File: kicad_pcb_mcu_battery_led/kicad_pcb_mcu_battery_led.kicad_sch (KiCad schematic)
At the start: 32 parts, among them J1 USB_B_Micro, J2 Test points, J3 USART, J4 ST-Link, J5 SWD, SW1 SW_Push, SW2 SW_SPDT, U1 STM32F030C6, Y1 32k, Y2 16M

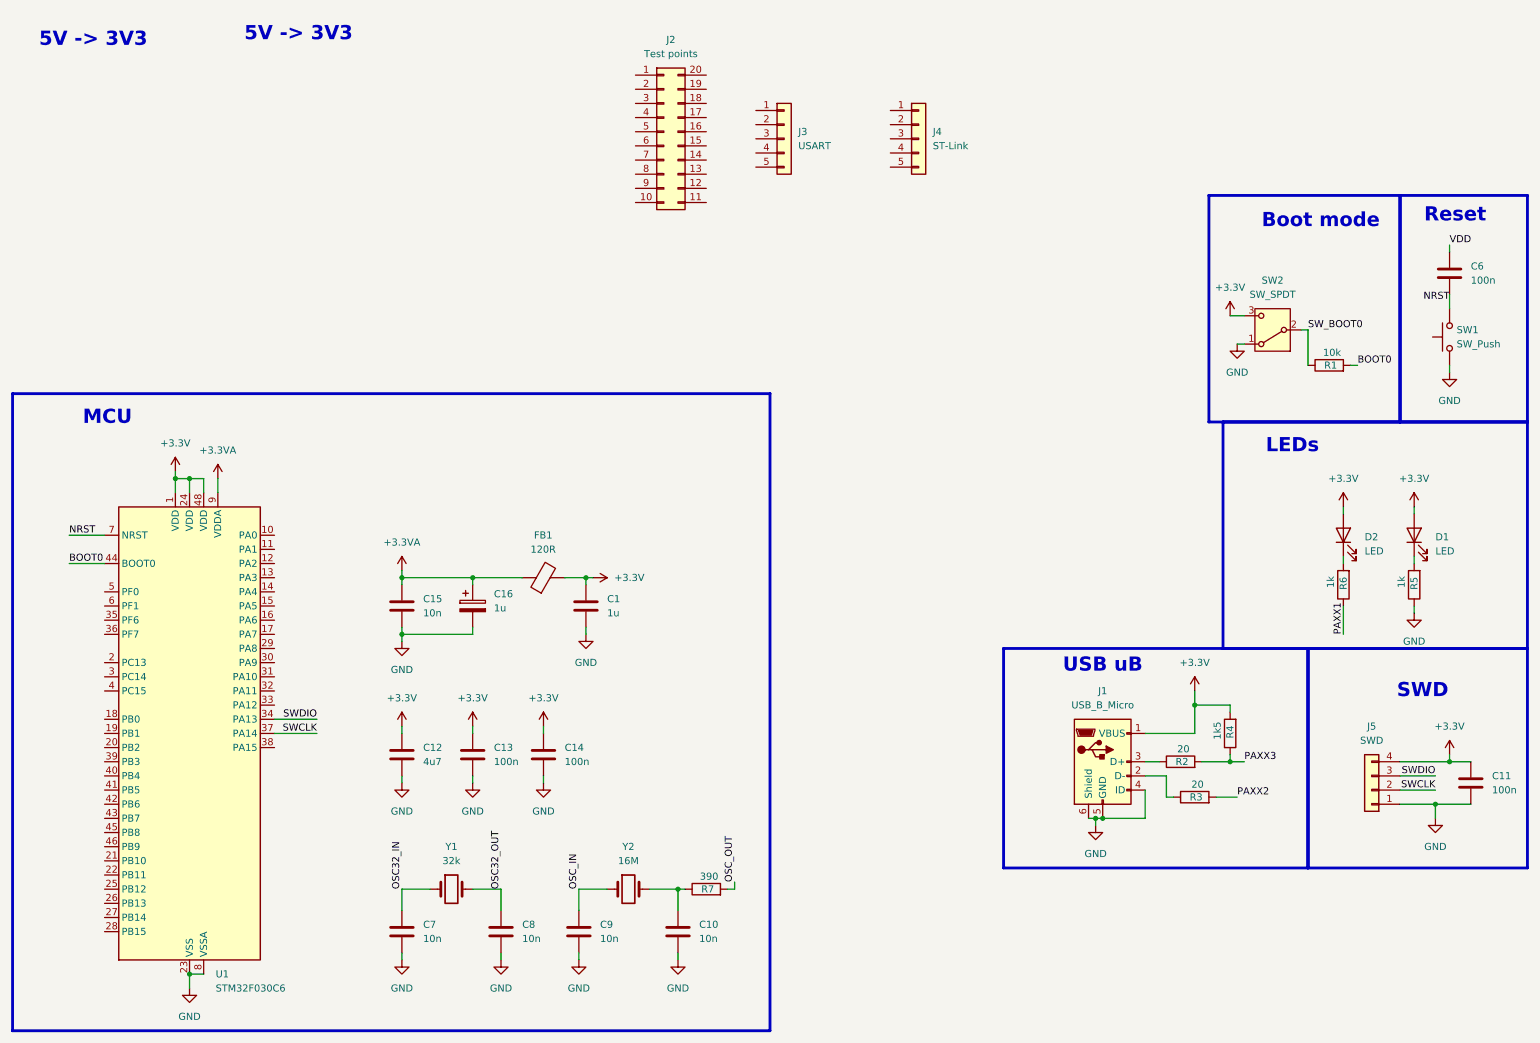
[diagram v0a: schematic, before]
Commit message: added atmega/esp32 project
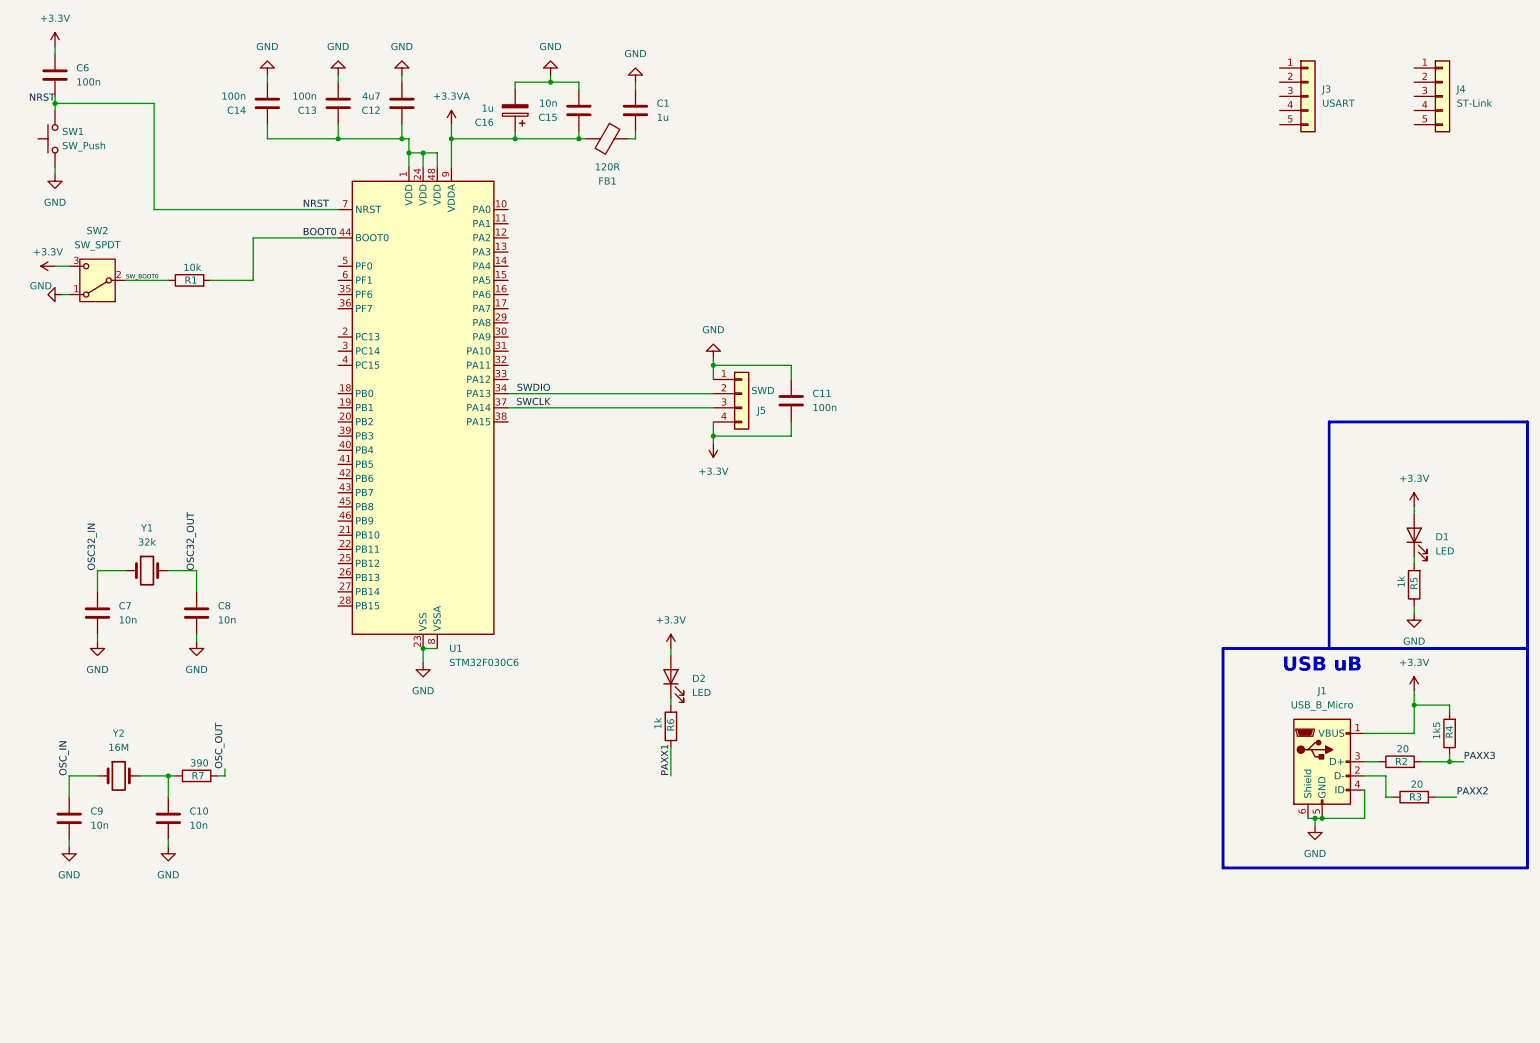
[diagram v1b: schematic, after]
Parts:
- removed J2: Test points, symbol Connector_Generic:Conn_02x10_Counter_Clockwise
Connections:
- net VDD is gone; now on net +3.3V: C6.1
- net +3.3V: now also C11.2; no longer C1.1, C11.1, C12.1, C13.1, C14.1, FB1.2, U1.1 (VDD), U1.24 (VDD), U1.48 (VDD)
- net +3.3VA: now also FB1.2; no longer FB1.1
- net GND: now also C1.1, C11.1; no longer C1.2, C11.2
- net SWCLK: now also J5.3 (Pin_3); no longer J5.2 (Pin_2)
- net SWDIO: now also J5.2 (Pin_2); no longer J5.3 (Pin_3)
- new net: C12.1, C13.1, C14.1, U1.1 (VDD), U1.24 (VDD), U1.48 (VDD)
- new net: C1.2, FB1.1
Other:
- note removed: "5V -> 3V3"
- note removed: "Boot mode"
- note removed: "LEDs"
- note removed: "MCU"
- note removed: "Reset"
- note removed: "SWD"
- moved on the sheet: C1, C10, C11, C12, C13, C14, C15, C16, C6, C7, C8, C9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
